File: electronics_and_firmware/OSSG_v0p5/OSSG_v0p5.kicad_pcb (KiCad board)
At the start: 4 copper layers, 93 x 10 mm, 75 parts, among them J1 Conn_01x05_Male, J2 Ext RGB, J3 USB_B_Micro, J4 Touch, J5 Ext. HUD (experimental), Q1 2SC4617R BR, Q2 2SC4617R BR, Q3 PMZ290UNE2YL, Q4 YJQD30P02A, SW1 SW_SPST, SW2 Power, U1 MP23DB01HPTR, U2 ESP32-PICO-D4, U3 CH9102F, U4 XC61CC3002MR, U5 AP5054HTC, U6 MAX17048, U7 NCP167BMX330TBG, U8 SY7088, U9 LY68L6400SLIT_PSRAM

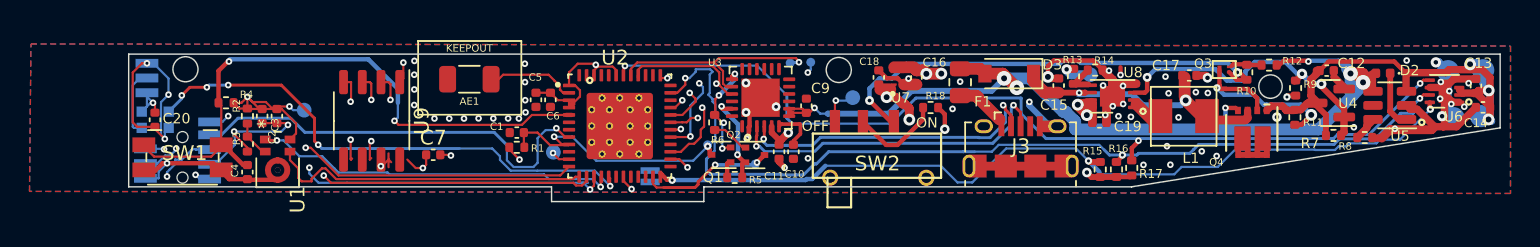
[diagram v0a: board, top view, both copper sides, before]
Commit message: move pcb shape notch to top, swap mic for i2s mic
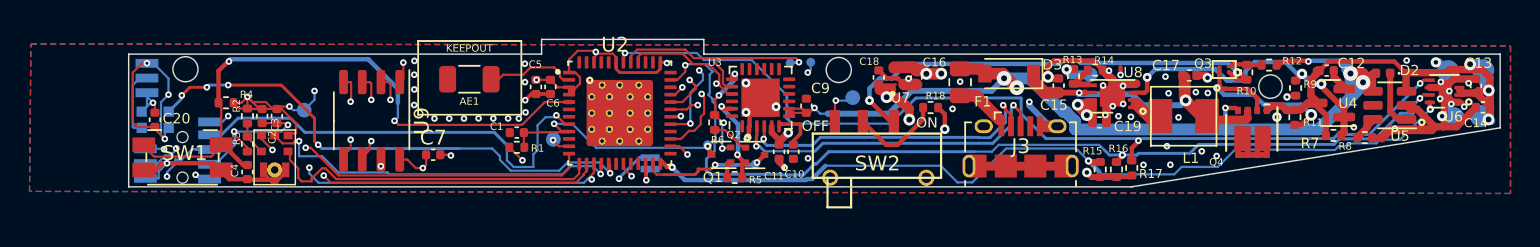
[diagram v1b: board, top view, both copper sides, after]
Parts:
- U1: value MP23DB01HPTR -> SPH0645LMH; footprint OSSG_footprints:MP23DB01HPTR -> OSSG_footprints:SPH0645LM4H-B-SMD-GND
- moved C5 0.88 mm to (94.6, 77.2)
- moved C6 0.88 mm to (95.6, 77.2)
- moved J4 0.88 mm to (102.3, 83.5)
- moved TP1 0.88 mm to (95.8, 80.8)
- moved U2 0.88 mm to (100.3, 79.0)
- moved U1 0.73 mm to (76.9, 82.8), turned to 0 degrees
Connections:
- U1 pad 1: i2S1_Data -> i2S2_WS
- U1 pad 6: (no net) -> i2S1_Data
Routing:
- net BATT1-: track 87.5 -> 94.9 mm, vias 65 -> 66
- net +3V3: track 40.7 -> 46.6 mm, vias 12 -> 14
- net i2S2_WS: track 26.5 -> 29.0 mm, vias 2 -> 3
- net TOUCH1: track 0.17 -> 2.17 mm, vias 0 -> 1
- net SCLK: track 28.8 -> 30.2 mm
- net SIO3: track 28.7 -> 27.3 mm
- net SIO0: track 28.2 -> 29.4 mm
- net PSRAM_CS: track 34.2 -> 35.4 mm
- net SIO2: track 29.9 -> 31.1 mm
- net +5V: track 100.5 -> 101.6 mm
- net VDD_SDIO: track 22.7 -> 23.6 mm
- net i2S2_Data: track 29.1 -> 30.0 mm
- net i2S1_CLK: track 22.0 -> 22.7 mm
- net EN: track 17.9 -> 17.2 mm
- net TX_ESP: track 16.1 -> 16.7 mm
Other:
- outline, holes or cut-outs redrawn

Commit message: fix issues, fix silk screen, add psram pullup, change i2s mic footprint, change battery charging resistor, make notch bigger and fix 3v3 pour not contiguous
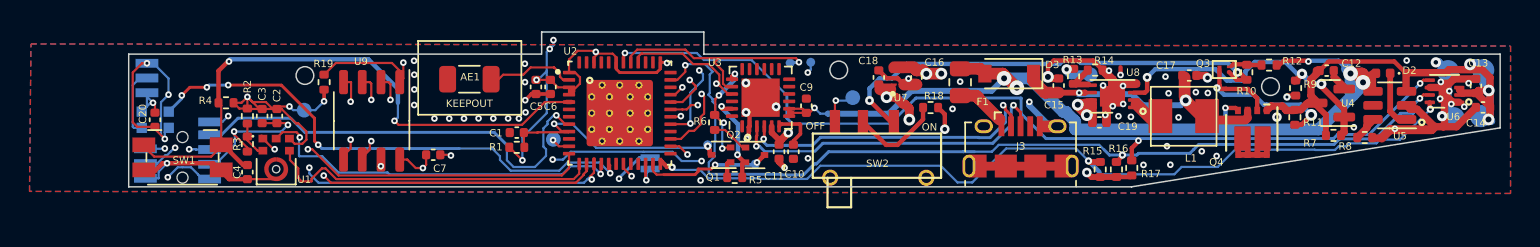
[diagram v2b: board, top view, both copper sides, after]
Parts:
- added R19: *10k, Resistor_SMD:R_0402_1005Metric, F.Cu at (80.2, 76.9)
- R8: value 2K -> 2.2K
- U1: footprint OSSG_footprints:SPH0645LM4H-B-SMD-GND -> OSSG_footprints:MIC_SPH0645LM4H-B
- moved U1 0.11 mm to (77.0, 82.8)
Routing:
- net +3V3: track 46.6 -> 80.2 mm, vias 14 -> 19
- net PSRAM_CS: track 35.4 -> 41.8 mm
- net i2S2_CLK: track 34.4 -> 31.0 mm
- net DAC: track 34.5 -> 36.9 mm
- net BATT1-: track 94.9 -> 93.5 mm
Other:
- board size 93 x 10 mm -> 93 x 10.5 mm
- board text added: "Design: Cayden Pierce, Paul Hamilton, Nicholas Gray"
- board text added: "M1"
- board text added: "Open Source Smart Glasses V0.5"
- board text removed: "Design: Cayden Pierce, Nicholas Gray, Paul Hamilton"
- board text removed: "M1.5"
- board text removed: "M1.6"
- board text removed: "Open Source Smart Glasses V0.4a"

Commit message: add mosfet switch for display power, thicken some traces, check things over
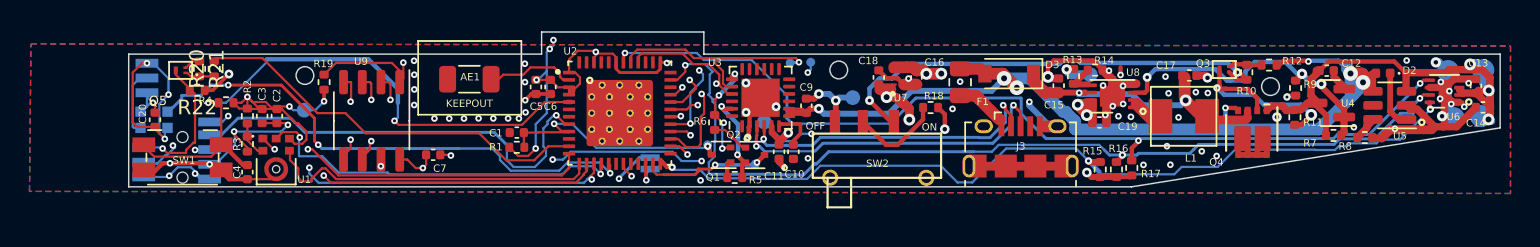
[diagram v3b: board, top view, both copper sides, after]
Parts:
- added Q5: PMZ290UNE2YL, OSSG_footprints:DFN100X60X40-3N, F.Cu at (70.5, 76.1)
- added R20: 10K, Resistor_SMD:R_0402_1005Metric, F.Cu at (72.8, 76.0)
- added R21: 100K, Resistor_SMD:R_0402_1005Metric, F.Cu at (71.8, 76.0)
- added R22: NC, Resistor_SMD:R_0402_1005Metric, F.Cu at (71.7, 77.5)
- J5: value Ext. HUD (experimental) -> Ext. HUD
- R8: value 2.2K -> 2.1k
- TP1: value IO35 -> IO9
- moved TP1 14.4 mm to (110.1, 79.6)
- moved J5 0.86 mm to (68.0, 82.8), turned to -90 degrees
- moved D1 0.08 mm to (68.7, 79.5)
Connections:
- net +3V3 renamed HUD+
- J5 pad 1: BATT1- -> HUD-
- TP1 pad 1: IO35 -> IO9
- U2 pad 11: IO35 -> DISPLAY_EN
- U2 pad 28: unconnected-(U2-Pad28) -> IO9
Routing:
- net DISPLAY_EN: track 0.00 -> 27.5 mm
- net IO9: track 0.00 -> 14.3 mm, vias 0 -> 2
- net HUD-: track 0.00 -> 9.50 mm, vias 0 -> 1
- net BATT1-: track 93.5 -> 100.0 mm, vias 66 -> 69
- net Net-(Q5-Pad1): track 0.00 -> 2.05 mm
- net BATT+: track 75.5 -> 77.0 mm
- net VBUS: track 65.3 -> 66.6 mm
- net IO35: track 1.27 -> 0.00 mm, vias 1 -> 0
- net SIO1: track 33.7 -> 34.9 mm
- net HUD+: track 80.2 -> 79.1 mm
- net +5V: track 101.6 -> 102.6 mm
- net i2S2_CLK: track 31.0 -> 30.3 mm
- net RGB: vias 5 -> 3

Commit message: change display MOSFET switch to p-type and switch high, thicken some traces on ext. i2s board, slide button down (check this fits capabilities), get rid of via in pad, move i2s line so not over top of psram lines
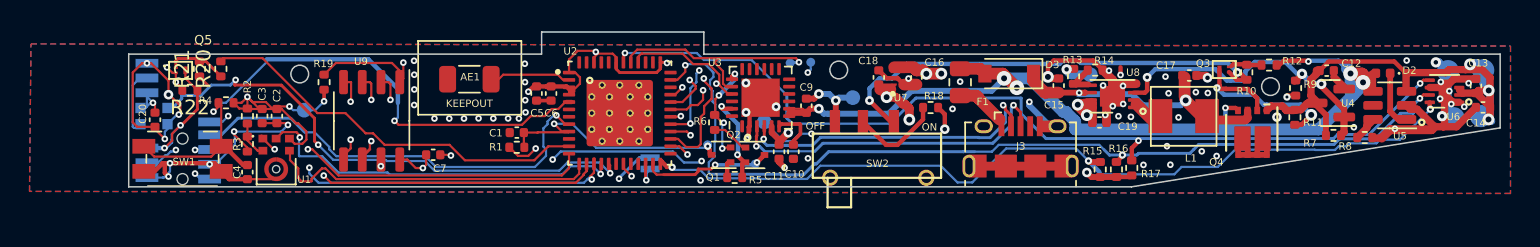
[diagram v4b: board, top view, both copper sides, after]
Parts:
- Q5: value PMZ290UNE2YL -> PMZ350UPEYL
- moved J5 0.93 mm to (68.2, 81.9), turned to 90 degrees
- moved R22 0.50 mm to (71.2, 77.5)
- moved R20 0.45 mm to (73.2, 76.0)
- moved C5 0.45 mm to (94.7, 77.7)
- moved C6 0.45 mm to (95.6, 77.7)
- moved D1 0.25 mm to (68.7, 79.2)
- moved SW1 0.10 mm to (70.7, 82.1)
- turned Q5 to 0 degrees
- turned R21 to 90 degrees
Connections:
- C11 pad 1: HUD+ -> +3V3
- C18 pad 2: HUD+ -> +3V3
- C2 pad 1: HUD+ -> +3V3
- C3 pad 2: HUD+ -> +3V3
- C5 pad 1: HUD+ -> +3V3
- C6 pad 1: HUD+ -> +3V3
- J1 pad 1: HUD+ -> +3V3
- J5 pad 1: HUD- -> BATT1-
- Q5 pad 2: BATT1- -> +3V3
- Q5 pad 3: HUD- -> HUD+
- R1 pad 2: HUD+ -> +3V3
- R15 pad 1: HUD+ -> +3V3
- R16 pad 1: HUD+ -> +3V3
- R17 pad 1: HUD+ -> +3V3
- R19 pad 1: HUD+ -> +3V3
- R2 pad 2: HUD+ -> +3V3
- R22 pad 1: BATT1- -> HUD+
- R22 pad 2: HUD- -> +3V3
- R4 pad 2: HUD+ -> +3V3
- TP8 pad 1: HUD+ -> +3V3
- U1 pad 5: HUD+ -> +3V3
- U2 pad 1: HUD+ -> +3V3
- U2 pad 19: HUD+ -> +3V3
- U2 pad 3: HUD+ -> +3V3
- U2 pad 37: HUD+ -> +3V3
- U2 pad 4: HUD+ -> +3V3
- U2 pad 43: HUD+ -> +3V3
- U2 pad 46: HUD+ -> +3V3
- U3 pad 5: HUD+ -> +3V3
- U7 pad 1: HUD+ -> +3V3
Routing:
- net HUD+: track 79.1 -> 9.76 mm, vias 19 -> 2
- net +3V3: track 0.00 -> 68.5 mm, vias 0 -> 18
- net HUD-: track 9.50 -> 0.00 mm, vias 1 -> 0
- net DAC: track 36.9 -> 34.8 mm
- net Net-(R20-Pad1): track 2.05 -> 4.11 mm
- net SCLK: track 30.2 -> 31.6 mm
- net Net-(AE1-Pad2): track 5.60 -> 4.63 mm
- net BATT1-: track 100.0 -> 100.6 mm
- net i2S2_Data: track 30.0 -> 29.5 mm
- net +5V: track 102.6 -> 102.3 mm, vias 8 -> 9
- added copper zone on In2.Cu, net +3V3
- removed copper zone on In2.Cu, net HUD+
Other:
- outline, holes or cut-outs redrawn

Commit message: final v0.5 PCB and components order files
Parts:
- moved TP17 0.29 mm to (156.6, 79.5)
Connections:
- Q5 pad 1: Net-(R20-Pad1) -> Net-(Q5-Pad1)
- R20 pad 1: Net-(R20-Pad1) -> Net-(Q5-Pad1)
- R21 pad 1: BATT1- -> Net-(Q5-Pad1)
- R21 pad 2: Net-(R20-Pad1) -> +3V3
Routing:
- net Net-(R20-Pad1): track 4.11 -> 0.00 mm
- net Net-(Q5-Pad1): track 0.00 -> 3.79 mm
- net +3V3: track 68.5 -> 71.6 mm
- net BATT1-: track 100.6 -> 99.7 mm
